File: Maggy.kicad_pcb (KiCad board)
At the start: 2 copper layers, 160 x 100 mm, 75 parts, among them CN1 0430450800, CN2 430451000, J1 XY308-2.54-2P, J2 XY308-2.54-2P, J3 XY308-2.54-2P, J4 XY308-2.54-2P, U1 CH224K, U10 INA214AIDCKR, U11 Socket for Teensy 4.1 (2x 1x2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, U12 INA214AIDCKR, U13 INA214AIDCKR, U14 TMAG5170A2DGKR, U15 TMAG5170A2DGKR, U16 TMAG5170A2DGKR, U17 TMAG5170A2DGKR, U18 TMAG5170A2DGKR, U2 A4950ELJTR-T, U3 A4950ELJTR-T, U4 A4950ELJTR-T, U5 A4950ELJTR-T, U6 TLV2372, U7 LM1117S-3.3, U8 LM1117S-5.0, U9 INA214AIDCKR

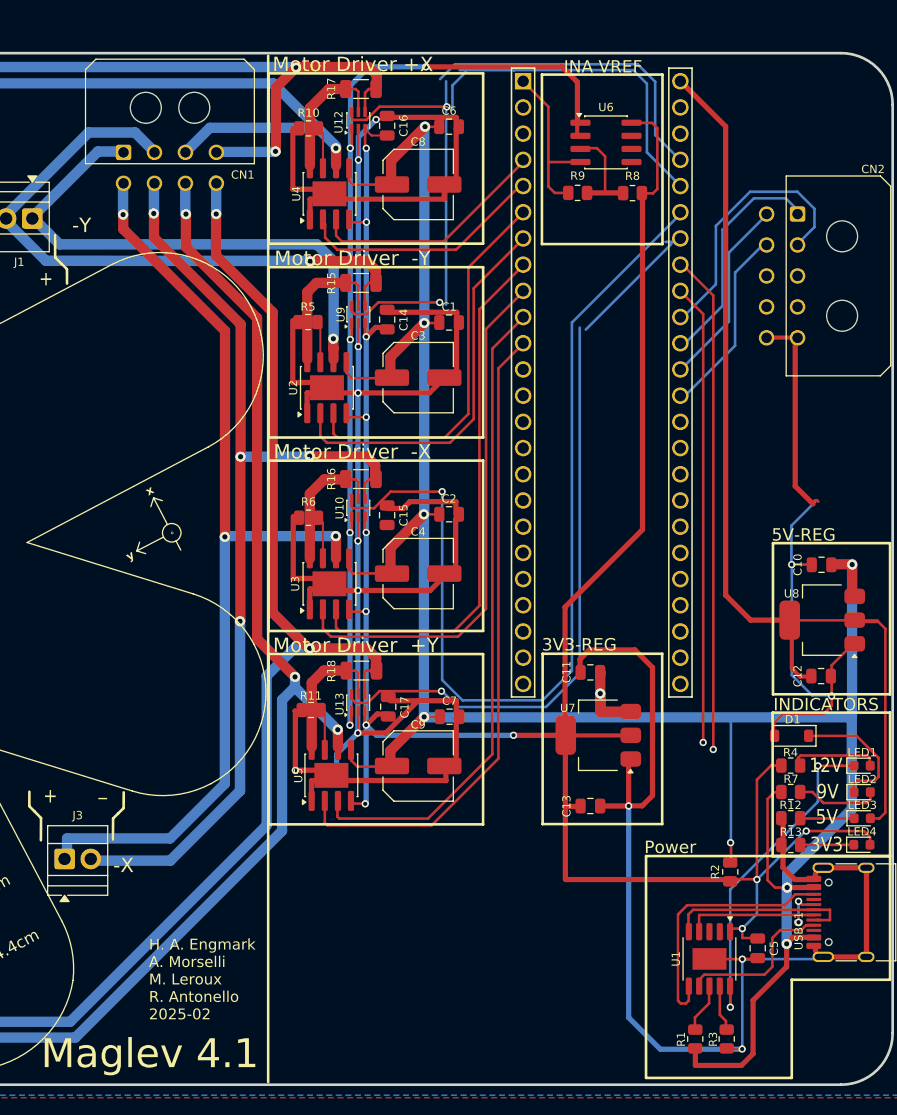
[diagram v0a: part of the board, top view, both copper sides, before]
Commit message: fix: routing for the motor drivers
Fixed routing for the motor drivers, clearing any DRC violations while at it
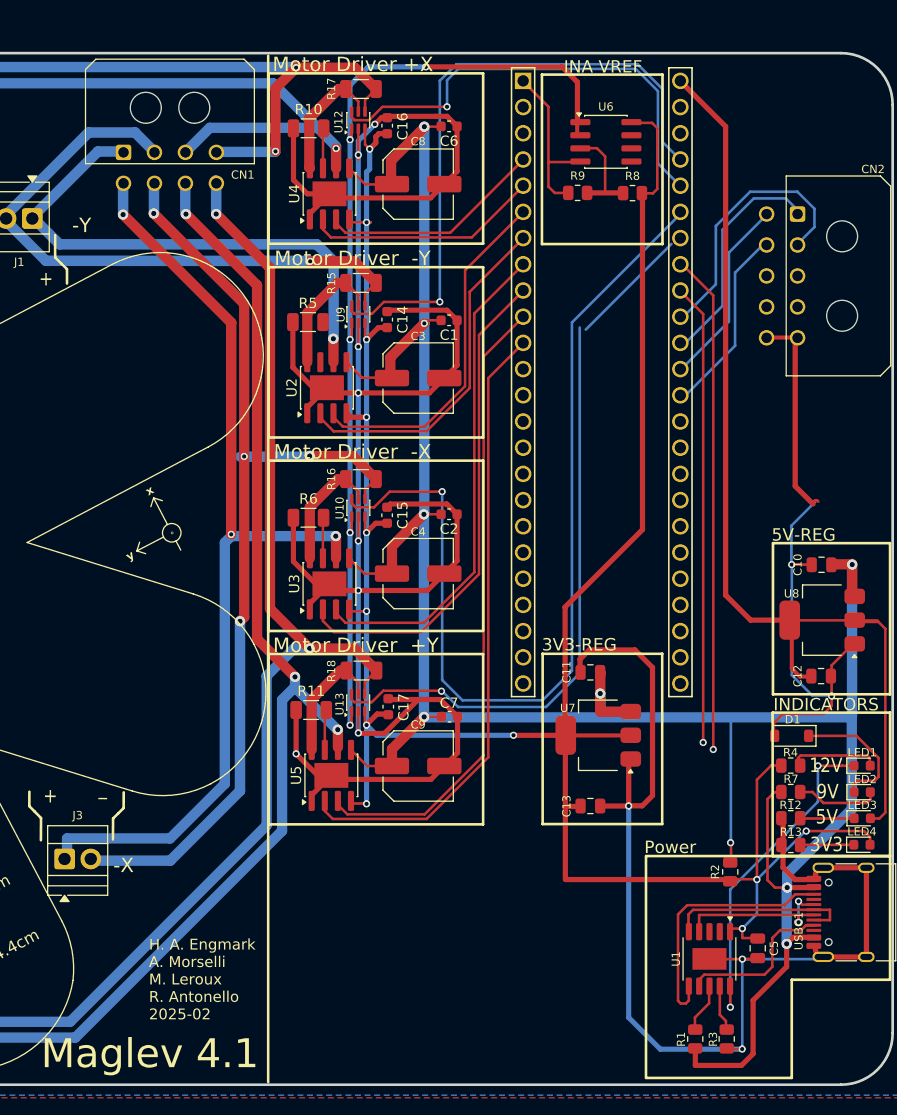
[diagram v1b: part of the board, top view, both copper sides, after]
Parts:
- C1, C14, C15, C16, C17, C2, C6, C7: footprint Capacitor_SMD:C_0805_2012Metric -> Capacitor_SMD:C_0603_1608Metric
- R10, R11, R5, R6: footprint Resistor_SMD:R_0805_2012Metric -> Resistor_SMD:R_1206_3216Metric
- moved C1 0.22 mm to (187.0, 85.9)
- moved U6 0.05 mm to (202.2, 68.6)
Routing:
- net CUR_SOL2: track 66.4 -> 44.9 mm
- net CUR_SOL1: track 40.5 -> 61.9 mm
- net +3V3: track 242.4 -> 247.6 mm
- net GND: track 434.2 -> 429.9 mm
- net Net-(U2-LSS): track 4.01 -> 0.00 mm
- net HB_0B: track 37.5 -> 33.9 mm
- net HB_0A: track 37.6 -> 34.3 mm
- net HB_3A: track 51.1 -> 48.0 mm
- net HB_3B: track 51.1 -> 48.3 mm
- net CUR_SOL3: track 72.1 -> 70.5 mm
- net HB_2B: track 62.7 -> 61.2 mm
- net 4_22: track 13.5 -> 12.0 mm
- net 1_22: track 13.8 -> 12.4 mm
- net HB_1A: track 23.1 -> 21.8 mm
- net HB_2A: track 62.5 -> 61.3 mm
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
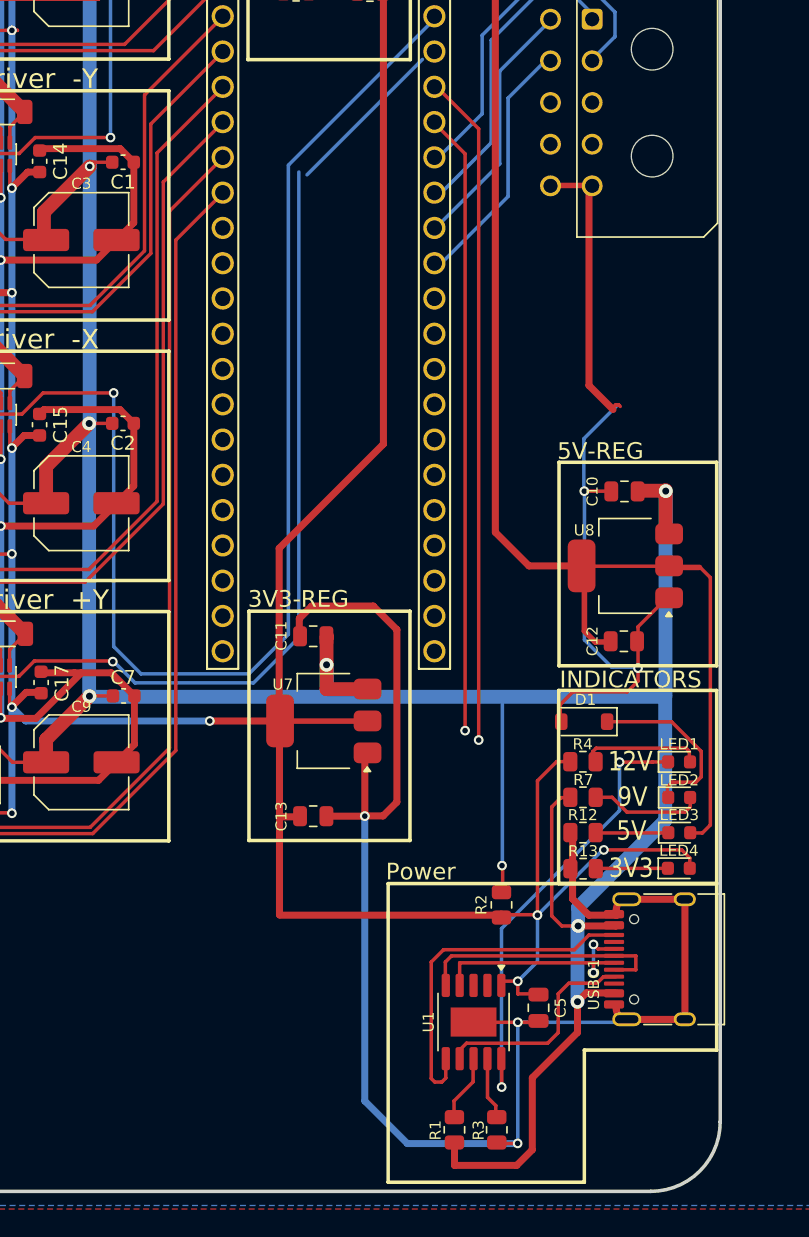
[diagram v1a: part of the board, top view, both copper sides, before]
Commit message: fix: fixed routing for USB-C and power management
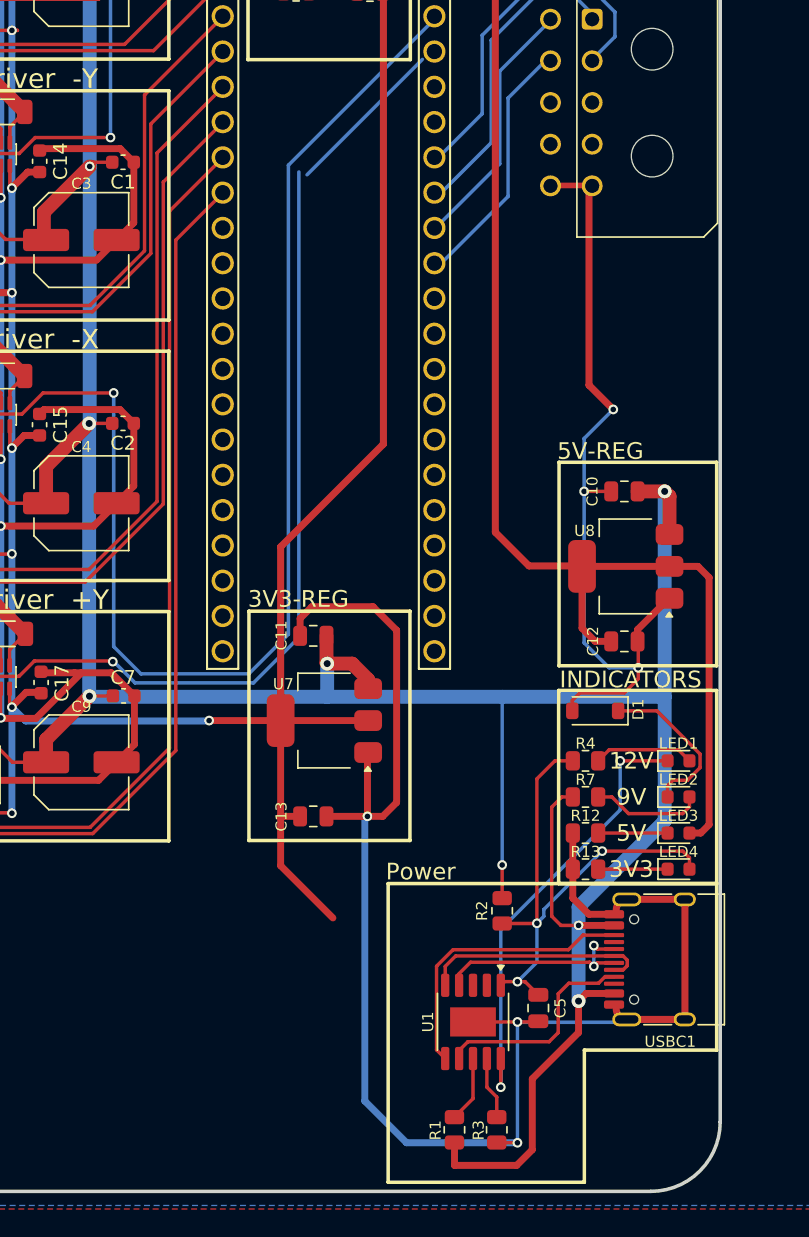
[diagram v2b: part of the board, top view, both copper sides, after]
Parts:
- moved D1 1.11 mm to (221.0, 125.4)
- moved R2 0.43 mm to (214.3, 139.8)
- moved R4 0.19 mm to (220.3, 129.0)
- moved R7 0.18 mm to (220.3, 131.6)
- moved R12 0.18 mm to (220.3, 134.2)
- moved R13 0.18 mm to (220.3, 136.8)
- moved LED1 0.09 mm to (227.0, 129.0)
- moved LED4 0.06 mm to (227.0, 136.8)
- moved LED2 0.06 mm to (227.0, 131.6)
- moved LED3 0.06 mm to (227.0, 134.2)
- moved U7 0.05 mm to (201.5, 126.1)
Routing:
- net unconnected-(U11-19_A5_SCL-Pad41): track 48.3 -> 0.00 mm, vias 1 -> 0
- net unconnected-(U11-18_A4_SDA-Pad40): track 44.6 -> 0.00 mm, vias 1 -> 0
- net +3V3: track 247.6 -> 236.4 mm
- net CC2: track 24.8 -> 20.6 mm
- net GND: track 429.9 -> 428.0 mm, vias 18 -> 19
- net Net-(LED1-A): track 8.71 -> 7.24 mm
- net Net-(D1-K): track 13.1 -> 11.9 mm
- net DM: track 17.6 -> 16.4 mm
- net DP: track 17.1 -> 15.8 mm
- net VBUS: track 254.7 -> 255.9 mm
- net Net-(U1-CFG1): track 3.77 -> 4.51 mm
- net +5V: track 94.5 -> 95.1 mm
- net Net-(LED1-K): track 32.0 -> 32.6 mm

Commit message: fix: routing for CN2
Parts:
- moved CN2 0.08 mm to (220.7, 75.6)
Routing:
- net UY_N_IN: track 0.00 -> 32.7 mm
- net UY_P_IN: track 0.00 -> 26.8 mm
- net UX_P_IN: track 0.00 -> 22.6 mm
- net UX_N_IN: track 0.00 -> 22.2 mm
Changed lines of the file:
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@@
 	(footprint "Connector_Molex:Molex_Micro-Fit_3.0_43045-1000_2x05_P3.00mm_Horizontal"
 		(layer "F.Cu")
-		(at 220.78 75.6 -90)
+		(at 220.7 75.6 -90)
 		(descr "Molex Micro-Fit 3.0 Connector System, 43045-1000 (alternative finishes: 43045-100x), 5 Pins per row (https://www.molex.com/pdm_docs/sd/430450201_sd.pdf)")
 		(tags "connector Molex Micro-Fit_3.0 horizontal")
 		(property "Reference" "CN2"
-			(at -4.34 -7.32 180)
+			(at -4.3 0 0)
 			(layer "F.SilkS")
 			(effects
@@
 	)
 	(segment
-		(start 220.551 87.829)
-		(end 220.551 101.951)
-		(width 0.508)
-		(layer "F.Cu")
-		(net "GND")
-	)
-	(segment
 		(start 181.128501 66.130499)
 		(end 185.687961 66.130499)
@@
 	)
 	(segment
+		(start 220.7 102.1)
+		(end 222.3 103.7)
+		(width 0.5)
+		(layer "F.Cu")
+		(net "GND")
+	)
+	(segment
 		(start 173.4985 113.922)
 		(end 173.4985 113.352)
@@
 	)
 	(segment
-		(start 220.551 101.951)
-		(end 222.3 103.7)
-		(width 0.508)
-		(layer "F.Cu")
-		(net "GND")
-	)
-	(segment
 		(start 224.1 122.3)
 		(end 224.1 120.45)
@@
 	)
 	(segment
-		(start 180.998 66.261)
-		(end 181.128501 66.130499)
+		(start 220.7 87.6)
+		(end 220.7 102.1)
 		(width 0.5)
 		(layer "F.Cu")
@@
 	)
 	(segment
-		(start 220.78 87.6)
-		(end 220.551 87.829)
-		(width 0.508)
+		(start 180.998 66.261)
+		(end 181.128501 66.130499)
+		(width 0.5)
 		(layer "F.Cu")
 		(net "GND")
@@
 	)
 	(segment
-		(start 220.7515 87.5715)
-		(end 217.8085 87.5715)
-		(width 0.4)
-		(layer "F.Cu")
-		(net "GND")
-	)
-	(segment
 		(start 220.78 87.6)
 		(end 220.7515 87.5715)
@@
 	)
 	(segment
+		(start 217.7 87.6)
+		(end 220.7 87.6)
+		(width 0.5)
+		(layer "F.Cu")
+		(net "GND")
+	)
+	(segment
 		(start 173.26 73.64)
 		(end 171.9155 72.2955)
@@
 	)
 	(segment
-		(start 214.726 81.28)
-		(end 214.726 88.3615)
-		(width 0.254)
+		(start 222.225 83.125)
+		(end 222.225 95.605)
+		(width 0.25)
 		(layer "B.Cu")
-		(net "UY_N_OUT")
+		(net "UY_N_IN")
 	)
 	(segment
-		(start 209.8315 93.2565)
-		(end 209.472 93.2565)
+		(start 220.7 81.6)
+		(end 222.225 83.125)
+		(width 0.25)
+		(layer "B.Cu")
+		(net "UY_N_IN")
+	)
+	(segment
+		(start 222.225 95.605)
+		(end 209.42 108.41)
+		(width 0.25)
+		(layer "B.Cu")
+		(net "UY_N_IN")
+	)
+	(segment
+		(start 221.775 93.515)
+		(end 209.42 105.87)
+		(width 0.25)
+		(layer "B.Cu")
+		(net "UY_P_IN")
+	)
+	(segment
+		(start 220.7 84.6)
+		(end 221.775 85.675)
+		(width 0.25)
+		(layer "B.Cu")
+		(net "UY_P_IN")
+	)
+	(segment
+		(start 221.775 85.675)
+		(end 221.775 93.515)
+		(width 0.25)
+		(layer "B.Cu")
+		(net "UY_P_IN")
+	)
+	(segment
+		(start 215.62801 86.67199)
+		(end 215.62801 97.12199)
+		(width 0.25)
+		(layer "B.Cu")
+		(net "UX_N_IN")
+	)
+	(segment
+		(start 217.7 84.6)
+		(end 215.62801 86.67199)
+		(width 0.25)
+		(layer "B.Cu")
+		(net "UX_N_IN")
+	)
+	(segment
+		(start 215.62801 97.12199)
+		(end 209.42 103.33)
+		(width 0.25)
+		(layer "B.Cu")
+		(net "UX_N_IN")
+	)
+	(segment
+		(start 215.17801 95.03199)
+		(end 209.42 100.79)
+		(width 0.25)
+		(layer "B.Cu")
+		(net "UX_P_IN")
+	)
+	(segment
+		(start 215.17801 84.12199)
+		(end 215.17801 95.03199)
+		(width 0.25)
+		(layer "B.Cu")
+		(net "UX_P_IN")
+	)
+	(segment
+		(start 217.7 81.6)
+		(end 215.17801 84.12199)
+		(width 0.25)
+		(layer "B.Cu")
+		(net "UX_P_IN")
+	)
+	(segment
+		(start 217.7 78.6)
+		(end 214.726 81.574)
 		(width 0.254)
 		(layer "B.Cu")
@@
 	)
 	(segment
-		(start 217.3795 78.6265)
-		(end 214.726 81.28)
+		(start 209.8315 93.2565)
+		(end 209.472 93.2565)
 		(width 0.254)
 		(layer "B.Cu")
@@
 	)
 	(segment
-		(start 217.739 78.6265)
-		(end 217.3795 78.6265)
+		(start 214.726 81.574)
+		(end 214.726 88.3615)
 		(width 0.254)
 		(layer "B.Cu")
@@
 	)
 	(segment
-		(start 209.472 90.6635)
-		(end 214.1245 86.0115)
+		(start 217.739 78.6265)
+		(end 217.3795 78.6265)
 		(width 0.254)
 		(layer "B.Cu")
-		(net "UY_P_OUT")
+		(net "UY_N_OUT")
 	)
 	(segment
-		(start 214.1245 79.3395)
-		(end 217.739 75.725)
+		(start 214.1245 79.1755)
+		(end 217.7 75.6)
 		(width 0.254)
 		(layer "B.Cu")
@@
 	)
 	(segment
-		(start 217.739 75.725)
-		(end 217.739 75.6265)
+		(start 214.1245 86.0115)
+		(end 214.1245 79.1755)
 		(width 0.254)
 		(layer "B.Cu")
@@
 	)
 	(segment
-		(start 214.1245 86.0115)
-		(end 214.1245 79.3395)
+		(start 209.472 90.7165)
+		(end 209.472 90.6635)
 		(width 0.254)
 		(layer "B.Cu")
@@
 	)
 	(segment
-		(start 209.472 90.7165)
-		(end 209.472 90.6635)
+		(start 217.739 75.725)
+		(end 217.739 75.6265)
 		(width 0.254)
 		(layer "B.Cu")
@@
 	)
 	(segment
-		(start 219.647 74.0775)
-		(end 220.787 75.2175)
+		(start 209.472 90.6635)
+		(end 214.1245 86.0115)
 		(width 0.254)
 		(layer "B.Cu")
-		(net "UX_N_OUT")
+		(net "UY_P_OUT")
 	)
 	(segment
-		(start 213.511 77.113)
-		(end 216.5465 74.0775)
+		(start 220.7 74.7)
+		(end 220.7 75.6)
 		(width 0.254)
 		(layer "B.Cu")
@@
 	)
 	(segment
-		(start 220.787 75.2175)
-		(end 220.787 75.5835)
+		(start 209.5305 88.118)
+		(end 209.89 88.118)
 		(width 0.254)
 		(layer "B.Cu")
@@
 	)
 	(segment
-		(start 209.472 88.1765)
-		(end 209.5305 88.118)
+		(start 216.5465 74.0775)
+		(end 220.0775 74.0775)
 		(width 0.254)
 		(layer "B.Cu")
@@
 	)
 	(segment
-		(start 209.89 88.118)
-		(end 213.511 84.4965)
+		(start 213.511 77.113)
+		(end 216.5465 74.0775)
 		(width 0.254)
 		(layer "B.Cu")
@@
 	)
 	(segment
-		(start 216.5465 74.0775)
-		(end 219.647 74.0775)
+		(start 209.89 88.118)
+		(end 213.511 84.4965)
 		(width 0.254)
 		(layer "B.Cu")
@@
 	)
 	(segment
-		(start 209.5305 88.118)
-		(end 209.89 88.118)
+		(start 209.472 88.1765)
+		(end 209.5305 88.118)
 		(width 0.254)
 		(layer "B.Cu")
@@
 	)
 	(segment
-		(start 209.705 85.563)
-		(end 212.8615 82.407)
+		(start 220.0775 74.0775)
+		(end 220.7 74.7)
 		(width 0.254)
 		(layer "B.Cu")
-		(net "UX_P_OUT")
+		(net "UX_N_OUT")
 	)
 	(segment
-		(start 222.419 76.86)
-		(end 220.7385 78.541)
+		(start 212.8615 82.407)
+		(end 212.8615 76.7565)
 		(width 0.254)
 		(layer "B.Cu")
@@
 	)
 	(segment
-		(start 209.5455 85.563)
-		(end 209.705 85.563)
+		(start 209.705 85.563)
+		(end 212.8615 82.407)
 		(width 0.254)
 		(layer "B.Cu")
@@
 	)
 	(segment
-		(start 220.7385 78.541)
-		(end 220.7385 78.6265)
+		(start 209.472 85.6365)
+		(end 209.5455 85.563)
 		(width 0.254)
 		(layer "B.Cu")
@@
 	)
 	(segment
-		(start 212.8615 82.407)
-		(end 212.8615 76.7565)
+		(start 220.7695 73.438)
+		(end 222.4 75.0685)
 		(width 0.254)
 		(layer "B.Cu")
@@
 	)
 	(segment
-		(start 220.7695 73.438)
-		(end 222.419 75.0875)
+		(start 209.5455 85.563)
+		(end 209.705 85.563)
 		(width 0.254)
 		(layer "B.Cu")
@@
 	)
 	(segment
-		(start 209.472 85.6365)
-		(end 209.5455 85.563)
+		(start 222.4 76.9)
+		(end 220.7 78.6)
 		(width 0.254)
 		(layer "B.Cu")
@@
 	)
 	(segment
-		(start 222.419 75.0875)
-		(end 222.419 76.86)
+		(start 222.4 75.0685)
+		(end 222.4 76.9)
 		(width 0.254)
 		(layer "B.Cu")

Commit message: fix: routing for CN1
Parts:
- moved CN1 0.22 mm to (155.4, 69.4)
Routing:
- net 4_1: track 94.3 -> 94.9 mm

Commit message: fix: routing for terminal blocks
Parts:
- moved J2 0.10 mm to (90.0, 81.3)
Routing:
- net 4_1: track 94.9 -> 89.8 mm
- net 1_1: track 52.1 -> 52.9 mm
- net 4_21: track 97.0 -> 96.1 mm
- net 2_21: track 126.9 -> 126.2 mm
